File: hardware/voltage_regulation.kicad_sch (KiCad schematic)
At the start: 29 parts, among them U4 TPS51388VABR, U5 LD39050PU33R

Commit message: fix bom
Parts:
- D5: value 3V3 LED -> 3V3_LED
- R22: footprint Resistor_SMD:R_0402_1005Metric -> Resistor_SMD:R_0603_1608Metric
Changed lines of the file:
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@@
 			)
 		)
-		(property "Footprint" "Resistor_SMD:R_0402_1005Metric"
+		(property "Footprint" "Resistor_SMD:R_0603_1608Metric"
 			(at 97.028 129.54 90)
 			(hide yes)
@@
 			)
 		)
-		(property "Value" "3V3 LED"
+		(property "Value" "3V3_LED"
 			(at 99.06 143.8274 90)
 			(show_name no)

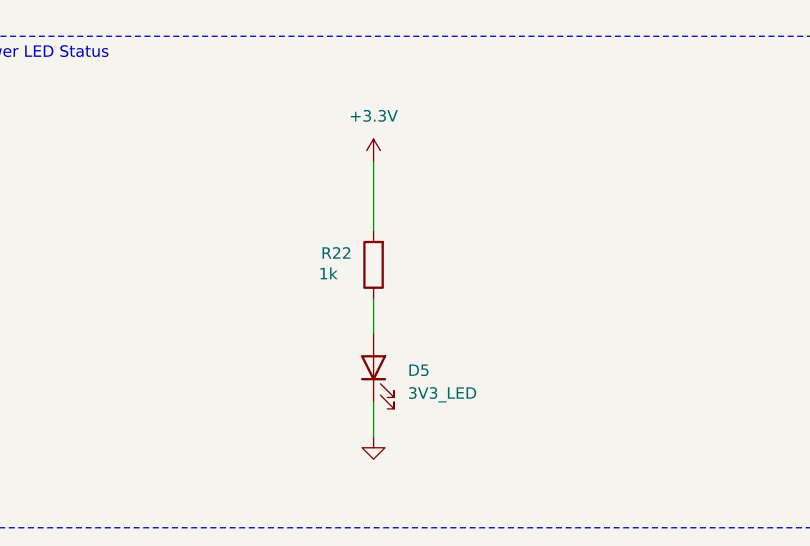
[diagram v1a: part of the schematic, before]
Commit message: bom optimisation for pcba
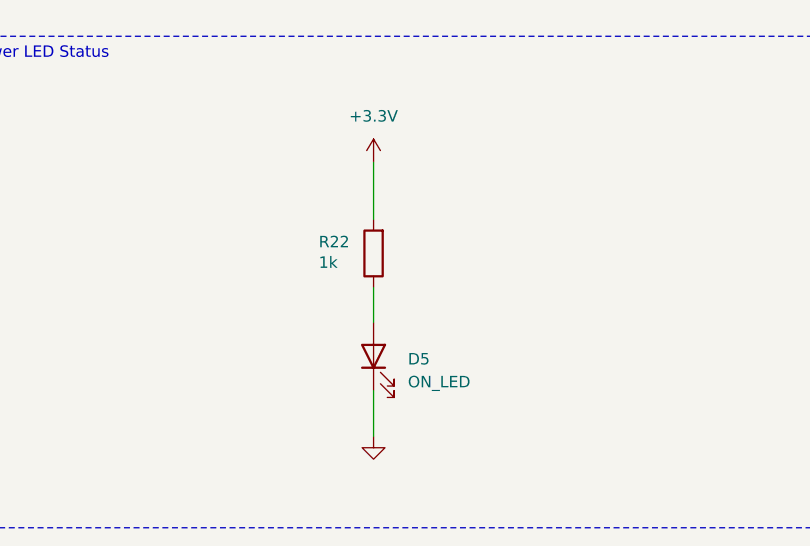
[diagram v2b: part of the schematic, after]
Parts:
- C10, C8, C9: JLCPCB Part # C69612 -> C12891; MPN C3216X5R1V226M160AC -> CL31A226KAHNNNE
- C11: JLCPCB Part # C1591 -> C14663; MPN CL10B104KB8NNNC -> CC0603KRX7R9BB104
- C12: JLCPCB Part # C2167658 -> C23630; MPN GRM188R71A225KE15J -> CL10A225KO8NNNC
- C7: JLCPCB Part # C1591 -> C14663
- D5: value 3V3_LED -> ON_LED; JLCPCB Part # C6650185 -> C2288; MPN 150060BS55040 -> KT-0603B
- R14, R16: JLCPCB Part # C844915 -> C21189; MPN CRCW06030000Z0EA -> 0603WAF0000T5E
- R17: JLCPCB Part # C844135 -> C21190; MPN (none) -> 0603WAF1001T5E
- R18: JLCPCB Part # C137797 -> C22872; MPN RC0603FR-07137KL -> 0603WAF1373T5E
- R22: JLCPCB Part # C844135 -> C21190; MPN CRCW06031K00JNEAC -> 0603WAF1001T5E
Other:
- moved on the sheet: D5, R22
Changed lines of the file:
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@@
 	(wire
 		(pts
-			(xy 95.25 133.35) (xy 95.25 137.16)
+			(xy 95.25 132.08) (xy 95.25 135.89)
 		)
 		(stroke
@@
 	(wire
 		(pts
-			(xy 95.25 144.78) (xy 95.25 148.59)
+			(xy 95.25 143.51) (xy 95.25 148.59)
 		)
 		(stroke
@@
 	(wire
 		(pts
-			(xy 95.25 118.11) (xy 95.25 125.73)
+			(xy 95.25 118.11) (xy 95.25 124.46)
 		)
 		(stroke
@@
 			)
 		)
-		(property "MPN" "C3216X5R1V226M160AC"
+		(property "MPN" "CL31A226KAHNNNE"
 			(at 83.82 49.53 0)
 			(hide yes)
@@
 			)
 		)
-		(property "JLCPCB Part #" "C69612"
+		(property "JLCPCB Part #" "C12891"
 			(at 83.82 49.53 0)
 			(hide yes)
@@
 	(symbol
 		(lib_id "Device:R")
-		(at 95.25 129.54 180)
+		(at 95.25 128.27 180)
 		(unit 1)
 		(body_style 1)
@@
 		(dnp no)
 		(property "Reference" "R22"
-			(at 89.408 128.27 0)
+			(at 89.154 127 0)
 			(show_name no)
 			(do_not_autoplace no)
@@
 		)
 		(property "Value" "1k"
-			(at 89.154 130.556 0)
+			(at 89.154 129.286 0)
 			(show_name no)
 			(do_not_autoplace no)
@@
 		)
 		(property "Footprint" "Resistor_SMD:R_0603_1608Metric"
-			(at 97.028 129.54 90)
+			(at 97.028 128.27 90)
 			(hide yes)
 			(show_name no)
@@
 		)
 		(property "Datasheet" ""
-			(at 95.25 129.54 0)
+			(at 95.25 128.27 0)
 			(hide yes)
 			(show_name no)
@@
 		)
 		(property "Description" "Resistor"
-			(at 95.25 129.54 0)
+			(at 95.25 128.27 0)
 			(hide yes)
 			(show_name no)
@@
 		)
 		(property "Author" ""
-			(at 95.25 129.54 0)
+			(at 95.25 128.27 0)
 			(hide yes)
 			(show_name no)
@@
 		)
 		(property "License" ""
-			(at 95.25 129.54 0)
+			(at 95.25 128.27 0)
 			(hide yes)
 			(show_name no)
@@
 		)
 		(property "MP" ""
-			(at 95.25 129.54 0)
+			(at 95.25 128.27 0)
 			(hide yes)
 			(show_name no)
@@
 			)
 		)
-		(property "MPN" "CRCW06031K00JNEAC"
-			(at 95.25 129.54 0)
+		(property "MPN" "0603WAF1001T5E"
+			(at 95.25 128.27 0)
 			(hide yes)
 			(show_name no)
@@
 			)
 		)
-		(property "JLCPCB Part #" "C844135"
-			(at 95.25 129.54 0)
+		(property "JLCPCB Part #" "C21190"
+			(at 95.25 128.27 0)
 			(hide yes)
 			(show_name no)
@@
 		)
 		(property "MANUFACTURER" ""
-			(at 95.25 129.54 0)
+			(at 95.25 128.27 0)
 			(hide yes)
 			(show_name no)
@@
 		)
 		(property "MAXIMUM_PACKAGE_HEIGHT" ""
-			(at 95.25 129.54 0)
+			(at 95.25 128.27 0)
 			(hide yes)
 			(show_name no)
@@
 		)
 		(property "PARTREV" ""
-			(at 95.25 129.54 0)
+			(at 95.25 128.27 0)
 			(hide yes)
 			(show_name no)
@@
 			)
 		)
-		(property "MPN" "CRCW06030000Z0EA"
+		(property "MPN" "0603WAF0000T5E"
 			(at 200.66 54.61 0)
 			(hide yes)
@@
 			)
 		)
-		(property "JLCPCB Part #" "C844915"
+		(property "JLCPCB Part #" "C21189"
 			(at 200.66 54.61 0)
 			(hide yes)
@@
 			)
 		)
-		(property "MPN" "CRCW06030000Z0EA"
+		(property "MPN" "0603WAF0000T5E"
 			(at 160.02 43.18 0)
 			(hide yes)
@@
 			)
 		)
-		(property "JLCPCB Part #" "C844915"
+		(property "JLCPCB Part #" "C21189"
 			(at 160.02 43.18 0)
 			(hide yes)
@@
 			)
 		)
-		(property "MPN" "C3216X5R1V226M160AC"
+		(property "MPN" "CL31A226KAHNNNE"
 			(at 77.47 49.53 0)
 			(hide yes)
@@
 			)
 		)
-		(property "JLCPCB Part #" "C69612"
+		(property "JLCPCB Part #" "C12891"
 			(at 77.47 49.53 0)
 			(hide yes)
@@
 			)
 		)
-		(property "MPN" "RC0603FR-07137KL"
+		(property "MPN" "0603WAF1373T5E"
 			(at 200.66 66.04 0)
 			(hide yes)
@@
 			)
 		)
-		(property "JLCPCB Part #" "C137797"
+		(property "JLCPCB Part #" "C22872"
 			(at 200.66 66.04 0)
 			(hide yes)
@@
 			)
 		)
-		(property "MPN" "CL10B104KB8NNNC"
+		(property "MPN" "CC0603KRX7R9BB104"
 			(at 90.17 49.53 0)
 			(hide yes)
@@
 			)
 		)
-		(property "JLCPCB Part #" "C1591"
+		(property "JLCPCB Part #" "C14663"
 			(at 90.17 49.53 0)
 			(hide yes)
@@
 	(symbol
 		(lib_id "Device:LED")
-		(at 95.25 140.97 90)
+		(at 95.25 139.7 90)
 		(unit 1)
 		(body_style 1)
@@
 		(fields_autoplaced yes)
 		(property "Reference" "D5"
-			(at 99.06 141.2874 90)
+			(at 99.06 140.0174 90)
 			(show_name no)
 			(do_not_autoplace no)
@@
 			)
 		)
-		(property "Value" "3V3_LED"
-			(at 99.06 143.8274 90)
+		(property "Value" "ON_LED"
+			(at 99.06 142.5574 90)
 			(show_name no)
 			(do_not_autoplace no)
@@
 		)
 		(property "Footprint" "LED_SMD:LED_0603_1608Metric"
-			(at 95.25 140.97 0)
+			(at 95.25 139.7 0)
 			(hide yes)
 			(show_name no)
@@
 		)
 		(property "Datasheet" ""
-			(at 95.25 140.97 0)
+			(at 95.25 139.7 0)
 			(hide yes)
 			(show_name no)
@@
 		)
 		(property "Description" "Light emitting diode (Blue)"
-			(at 95.25 140.97 0)
+			(at 95.25 139.7 0)
 			(hide yes)
 			(show_name no)
@@
 			)
 		)
-		(property "MPN" "150060BS55040"
-			(at 95.25 140.97 90)
+		(property "MPN" "KT-0603B"
+			(at 95.25 139.7 90)
 			(hide yes)
 			(show_name no)
@@
 			)
 		)
-		(property "JLCPCB Part #" "C6650185"
-			(at 95.25 140.97 90)
+		(property "JLCPCB Part #" "C2288"
+			(at 95.25 139.7 90)
 			(hide yes)
 			(show_name no)
@@
 		)
 		(property "MANUFACTURER" ""
-			(at 95.25 140.97 90)
+			(at 95.25 139.7 90)
 			(hide yes)
 			(show_name no)
@@
 		)
 		(property "MAXIMUM_PACKAGE_HEIGHT" ""
-			(at 95.25 140.97 90)
+			(at 95.25 139.7 90)
 			(hide yes)
 			(show_name no)
@@
 		)
 		(property "PARTREV" ""
-			(at 95.25 140.97 90)
+			(at 95.25 139.7 90)
 			(hide yes)
 			(show_name no)
@@
 			)
 		)
-		(property "JLCPCB Part #" "C1591"
+		(property "JLCPCB Part #" "C14663"
 			(at 168.91 43.18 0)
 			(hide yes)
@@
 			)
 		)
-		(property "MPN" ""
+		(property "MPN" "0603WAF1001T5E"
 			(at 172.72 60.96 0)
 			(hide yes)
@@
 			)
 		)
-		(property "JLCPCB Part #" "C844135"
+		(property "JLCPCB Part #" "C21190"
 			(at 172.72 60.96 0)
 			(hide yes)
@@
 			)
 		)
-		(property "MPN" "C3216X5R1V226M160AC"
+		(property "MPN" "CL31A226KAHNNNE"
 			(at 71.12 49.53 0)
 			(hide yes)
@@
 			)
 		)
-		(property "JLCPCB Part #" "C69612"
+		(property "JLCPCB Part #" "C12891"
 			(at 71.12 49.53 0)
 			(hide yes)
@@
 			)
 		)
-		(property "MPN" "GRM188R71A225KE15J"
+		(property "MPN" "CL10A225KO8NNNC"
 			(at 100.33 50.8 0)
 			(hide yes)
@@
 			)
 		)
-		(property "JLCPCB Part #" "C2167658"
+		(property "JLCPCB Part #" "C23630"
 			(at 100.33 50.8 0)
 			(hide yes)
